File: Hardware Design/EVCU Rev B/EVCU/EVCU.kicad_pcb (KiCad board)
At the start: 4 copper layers, 80.3 x 86.8 mm, 82 parts, among them J1 Conn_01x06, J2 Conn_01x02, J3 APPS/BSE_Conn, J4 Micro_SD_Card, J5 DB9_Male, J6 Conn_01x02, Q1 Q_PMOS_GSD, U1 AZ1117-3.3, U10 EMIF06-MSD02N16, U11 ESDALC6V1W5, U2 AP62250WU-7, U3 STM32L4R9ZITx, U4 LMV321, U5 MPU-6500, U6 SN65HVD230, U7 LMV321, U8 LMV321, U9 ESDCAN24-2BLY, X1 ECS-2520MV-160-CN-TR

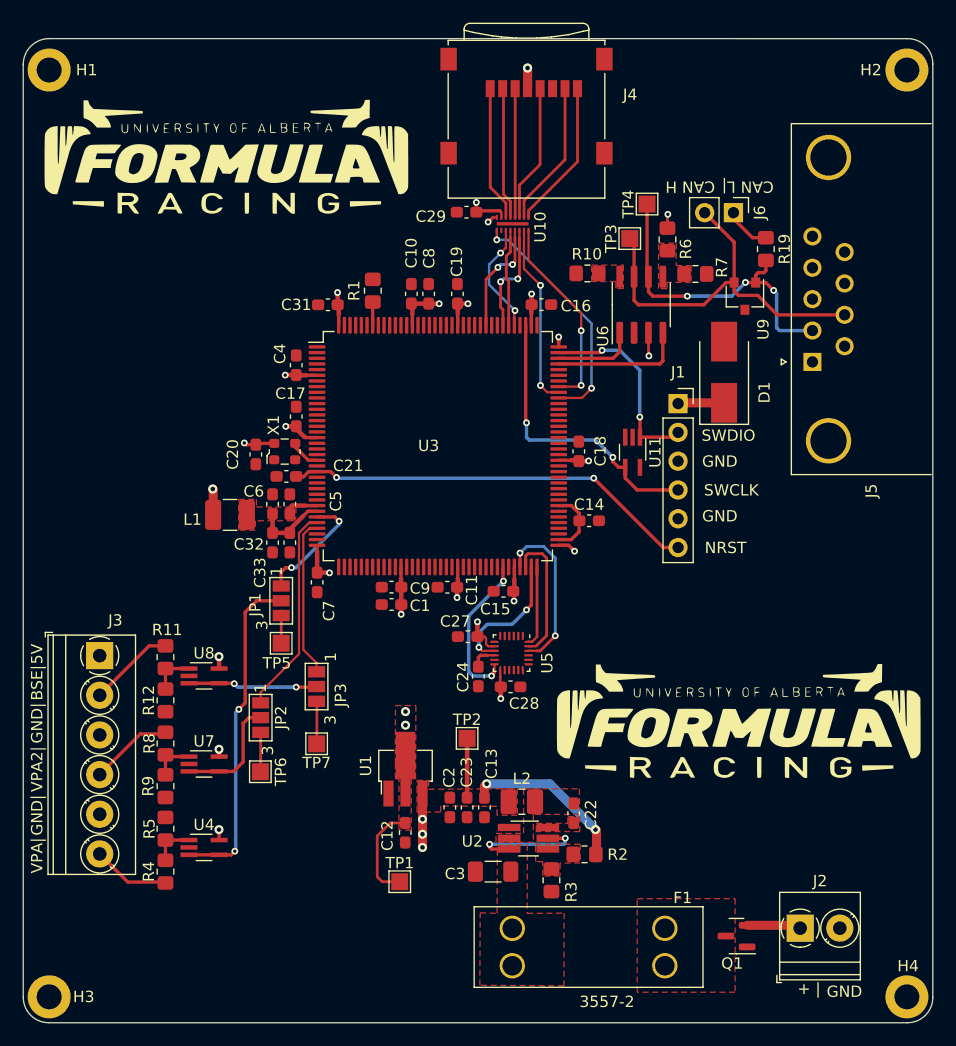
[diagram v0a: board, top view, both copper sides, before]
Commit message: 4 layer finished, gnd vias
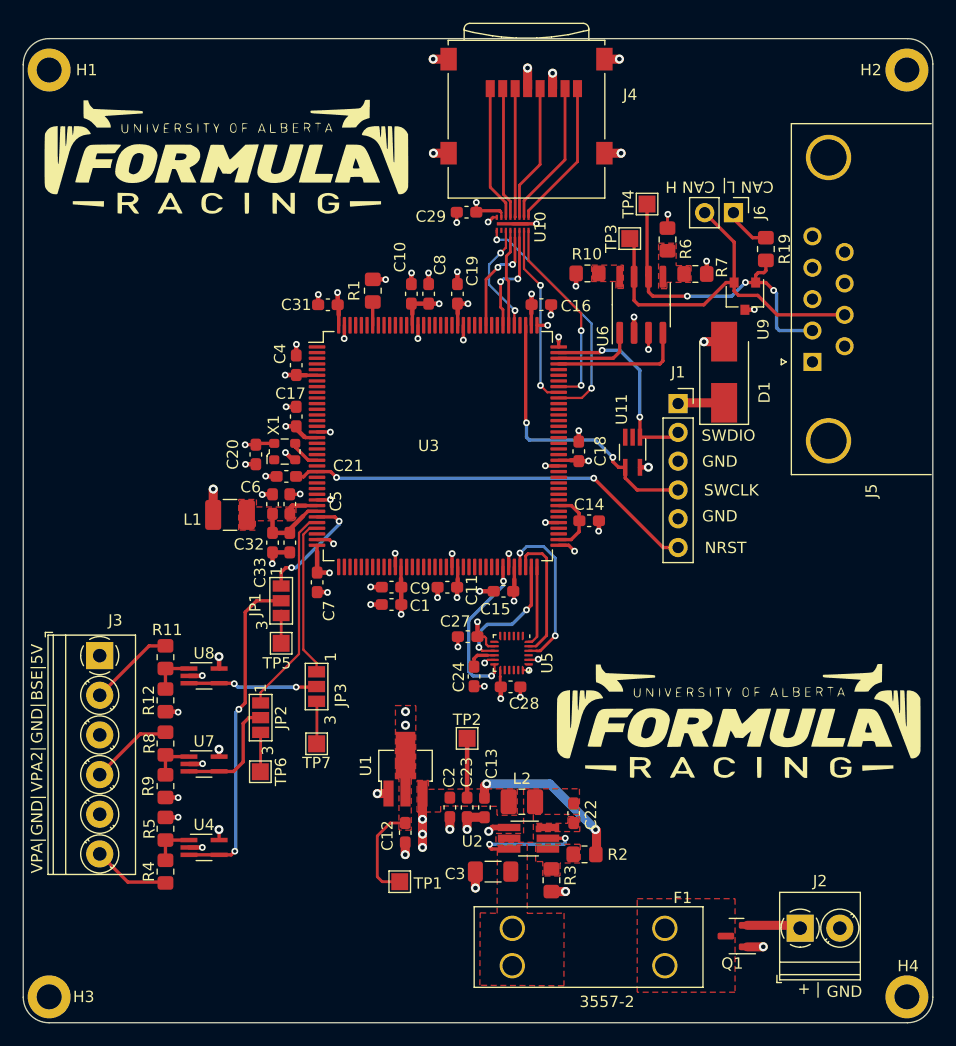
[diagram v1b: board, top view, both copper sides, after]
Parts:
- moved C24 0.38 mm to (121.3, 99.0)
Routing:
- net GND: track 0.23 -> 77.6 mm, vias 0 -> 66
- net +3V3: track 71.7 -> 70.9 mm

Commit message: fixed some silkscreen shit
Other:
- board text added: "CAN H|"
- board text added: "CAN L"
- board text removed: "CAN H"
- board text removed: "CAN L|"
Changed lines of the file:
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@@
     (property "Tolerance" "5%")
     (attr smd)
-    (fp_text reference "C21" (at -5.461 0.9398) (layer "F.SilkS")
-      (effects (font (size 1 1) (thickness 0.15)))
+    (fp_text reference "C21" (at 3.4036 -0.3302) (layer "F.SilkS")
+      (effects (font (size 0.9 0.9) (thickness 0.15)))
     )
     (fp_text value "0.1uF" (at 0 1.43) (layer "F.Fab")
@@
     (property "Tolerance" "5%")
     (attr smd)
-    (fp_text reference "C5" (at 0.254 4.064 90) (layer "F.SilkS")
-      (effects (font (size 1 1) (thickness 0.15)))
+    (fp_text reference "C5" (at -0.1778 0.9906 90) (layer "F.SilkS")
+      (effects (font (size 0.8 0.8) (thickness 0.15)))
     )
     (fp_text value "1uF" (at 0 1.43 90) (layer "F.Fab")
@@
     (property "Tolerance" "5%")
     (attr smd)
-    (fp_text reference "C6" (at 1.4986 -1.9304 180) (layer "F.SilkS")
-      (effects (font (size 1 1) (thickness 0.15)))
+    (fp_text reference "C6" (at 1.0922 -2.1844 180) (layer "F.SilkS")
+      (effects (font (size 0.9 0.9) (thickness 0.15)))
     )
     (fp_text value "10nF" (at 0 1.43 90) (layer "F.Fab")
@@
     (effects (font (size 1 1) (thickness 0.15)))
   )
-  (gr_text "CAN L|\n" (at 145.469531 55.7692 180) (layer "F.SilkS")
+  (gr_text "CAN L\n" (at 145.469531 55.7692) (layer "F.SilkS")
     (effects (font (size 1 1) (thickness 0.15)))
   )
-  (gr_text "CAN H\n" (at 140.389531 55.7692 180) (layer "F.SilkS")
+  (gr_text "CAN H|\n" (at 140.389531 55.7692) (layer "F.SilkS")
     (effects (font (size 1 1) (thickness 0.15)))
   )
